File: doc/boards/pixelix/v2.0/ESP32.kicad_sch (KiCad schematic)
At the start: 4 parts

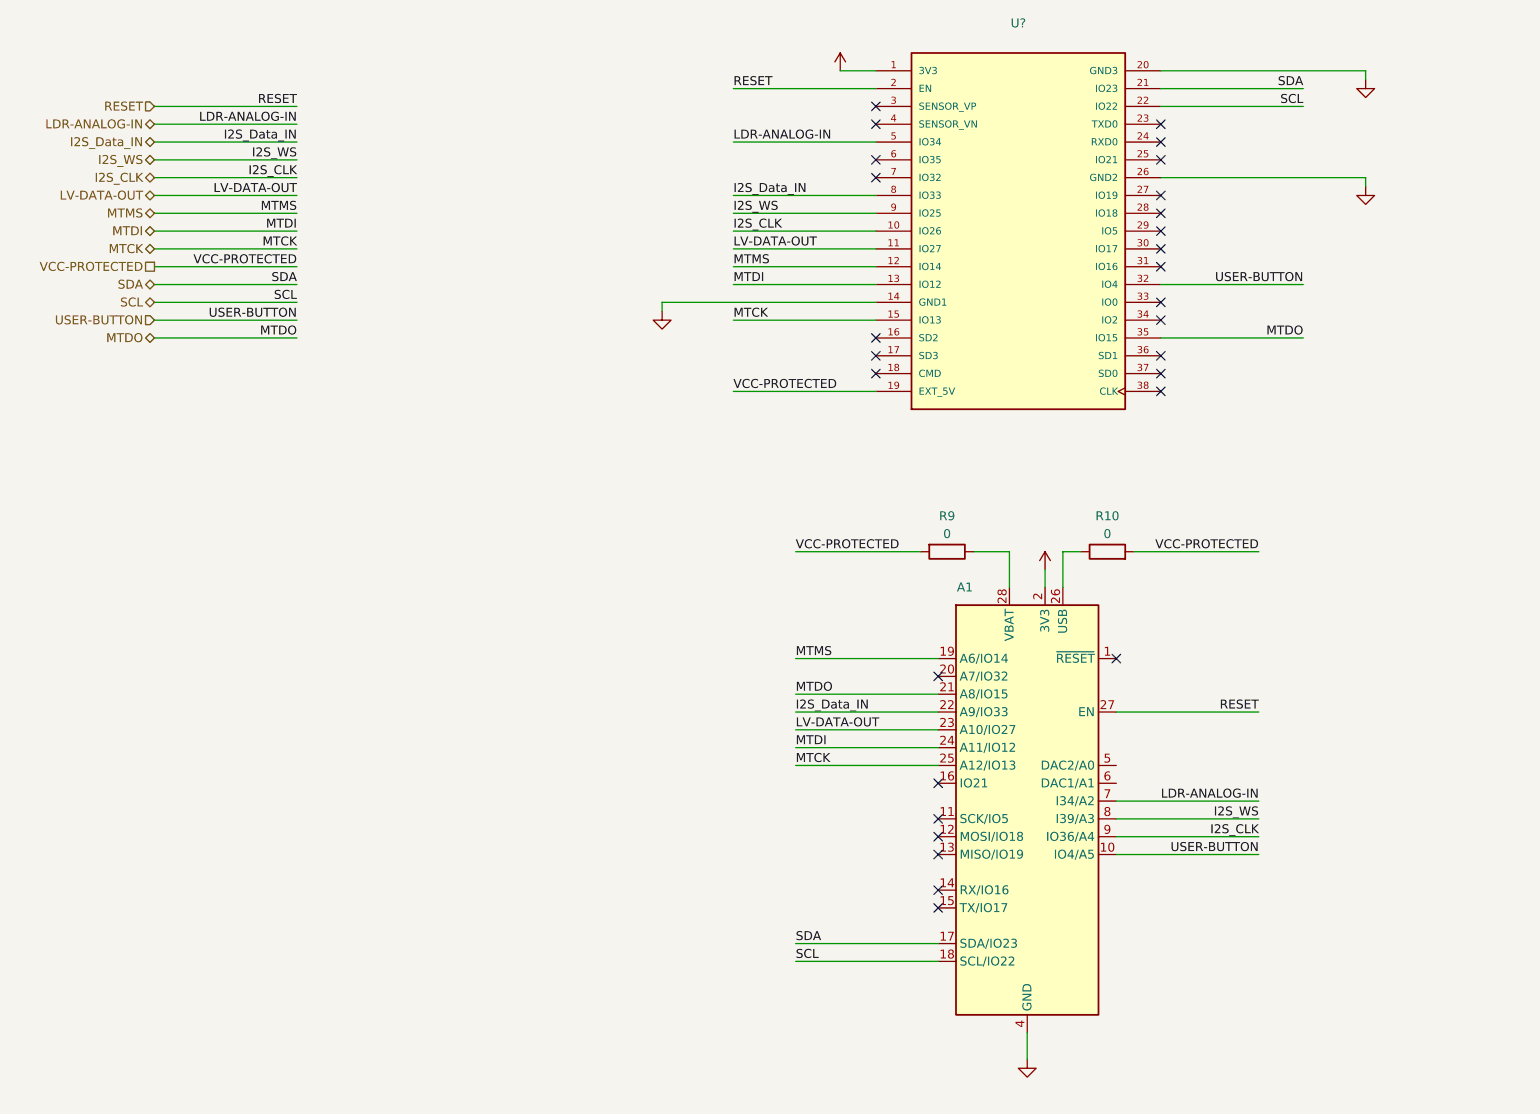
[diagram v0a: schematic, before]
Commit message: Board v2.0 Schematic - add Components (similar to v1.5) - add Pixelix Logo in header
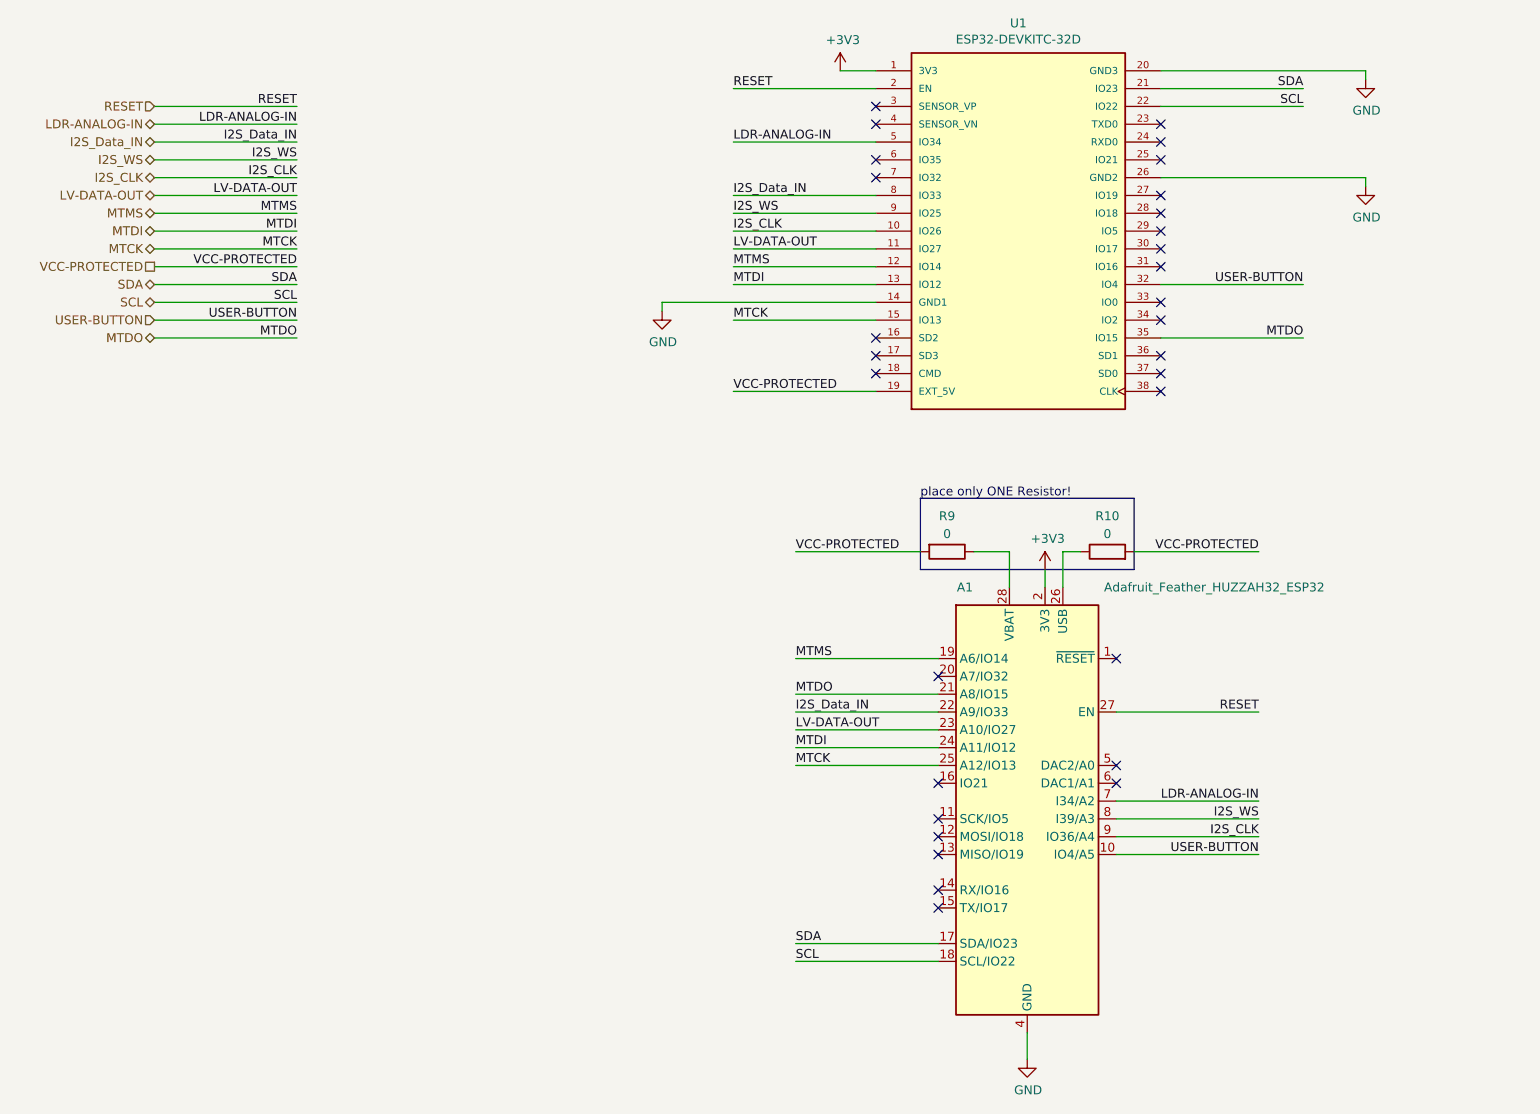
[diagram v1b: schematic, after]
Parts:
- A1: value (none) -> Adafruit_Feather_HUZZAH32_ESP32; footprint (none) -> Module:Adafruit_Feather; Manufacturer (none) -> Adafruit Feather; Part-No. (none) -> HUZZAH32
- R10, R9: footprint (none) -> Resistor_SMD:R_1206_3216Metric_Pad1.30x1.75mm_HandSolder; Manufacturer (none) -> -; Part-No. (none) -> -
- U1: renamed from U?; value (none) -> ESP32-DEVKITC-32D; footprint (none) -> footprints:MODULE_ESP32-DEVKITC-32D; Part-No. (none) -> ESP32-DEVKITC-32D
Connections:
- no-connect marks 28 -> 30
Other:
- note added: "place only ONE Resistor!"
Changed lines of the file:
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@@
   (title_block
     (title "Pixelix")
-    (date "2022-08-05")
+    (date "2022-08-08")
     (rev "2.0")
     (comment 1 "Schneider, Niklas")
@@
   (no_connect (at 139.7 30.48))
   (no_connect (at 180.34 66.04))
+  (no_connect (at 173.99 121.92))
+  (no_connect (at 173.99 124.46))
   (no_connect (at 180.34 55.88))
   (no_connect (at 139.7 60.96))
@@
   (no_connect (at 180.34 40.64))
   (no_connect (at 180.34 35.56))
+  (polyline (pts (xy 146.05 93.98) (xy 176.53 93.98))
+    (stroke (width 0) (type default) (color 0 0 0 0))
+  )
   (wire (pts (xy 57.15 60.96) (xy 36.83 60.96))
     (stroke (width 0) (type default) (color 0 0 0 0))
@@
     (stroke (width 0) (type default) (color 0 0 0 0))
   )
+  (polyline (pts (xy 146.05 83.82) (xy 146.05 93.98))
+    (stroke (width 0) (type default) (color 0 0 0 0))
+  )
   (wire (pts (xy 209.55 38.1) (xy 180.34 38.1))
     (stroke (width 0) (type default) (color 0 0 0 0))
@@
     (stroke (width 0) (type default) (color 0 0 0 0))
   )
+  (polyline (pts (xy 146.05 83.82) (xy 176.53 83.82))
+    (stroke (width 0) (type default) (color 0 0 0 0))
+  )
   (wire (pts (xy 109.22 55.88) (xy 139.7 55.88))
     (stroke (width 0) (type default) (color 0 0 0 0))
@@
     (stroke (width 0) (type default) (color 0 0 0 0))
   )
+  (polyline (pts (xy 176.53 93.98) (xy 176.53 83.82))
+    (stroke (width 0) (type default) (color 0 0 0 0))
+  )
   (wire (pts (xy 128.27 106.68) (xy 148.59 106.68))
     (stroke (width 0) (type default) (color 0 0 0 0))
@@
     (stroke (width 0) (type default) (color 0 0 0 0))
   )
+  (image (at 261.62 173.99) (scale 1.81836)
+    (data
+      iVBORw0KGgoAAAANSUhEUgAAAUoAAABGCAYAAACqnN3KAAAABHNCSVQICAgIfAhkiAAAAAlwSFlz
+      AAAuGAAALhgBKqonIAAAAXpJREFUeJzt3cFqwzAQRVEp///P6io7lzfGE6Sm56zN2NDmgsGDxgAA
+      AAAAAAAAAAAAAAAAaDd3P0CnNcZK18wxZvd15edbhXnzxt+kMG9snbcK8+Zsv66sMG/cmddrFZ5v
+      3ni+9v/n5nkne+1+AIDTCSVAIJQAgVACBEIJEAglQCCUAIFQAgDwzFd8Nf92+uaBzZyrefs2X2zm
+      XM2zmXPFqzdAIJQAgVACBEIJEAglQCCUAIFQAgRCCQDAM1u/ml+FzY15Y3Nj11k4Ve2bOeUbN2/c
+      lO/rzJwnujdz6vfd9fvo7UEnr94AgVACBEIJEAglQCCUAIFQAgRCCRAIJQAAz3zFeRZvp5/h4cyc
+      q3nOzPmNM3PO4dUbIBBKgEAoAQKhBAiEEiAQSoBAKAECoQQA4JlbX823n3Gz6cyc6rxuNnOu5v2F
+      M3O6r6v5b5s5J/fFqzdAIJQAgVACBEIJEAglQCCUAIFQAgRCCQAAAAAAAAAAAAAAAAB8wA+7/5tW
+      3HfTzAAAAABJRU5ErkJggg==
+    )
+  )
+  (text "place only ONE Resistor!" (at 146.05 83.82 0)
+    (effects (font (size 1.27 1.27)) (justify left bottom))
+  )
   (label "MTMS" (at 119.38 50.8 0)
     (effects (font (size 1.27 1.27)) (justify left bottom))
@@
   (symbol (lib_id "ESP32-DEVKITC-32D_new:ESP32-DEVKITC-32D") (at 160.02 45.72 0) (unit 1)
     (in_bom yes) (on_board yes)
-    (property "Reference" "U?" (id 0) (at 160.02 16.0782 0))
-    (property "Value" "" (id 1) (at 160.02 18.3896 0))
-    (property "Footprint" "" (id 2) (at 160.02 45.72 0)
+    (property "Reference" "U1" (id 0) (at 160.02 16.0782 0))
+    (property "Value" "ESP32-DEVKITC-32D" (id 1) (at 160.02 18.3896 0))
+    (property "Footprint" "footprints:MODULE_ESP32-DEVKITC-32D" (id 2) (at 160.02 45.72 0)
       (effects (font (size 1.27 1.27)) (justify left bottom) hide)
     )
@@
     )
     (property "Manufacturer" "Espressif Systems" (id 4) (at 160.02 45.72 0)
+      (effects (font (size 1.27 1.27)) hide)
+    )
+    (property "Part-No." "ESP32-DEVKITC-32D" (id 5) (at 160.02 45.72 0)
       (effects (font (size 1.27 1.27)) hide)
     )
@@
       (effects (font (size 1.27 1.27)) hide)
     )
-    (property "Value" "" (id 1) (at 135.001 18.4658 0))
+    (property "Value" "+3V3" (id 1) (at 135.001 18.4658 0))
     (property "Footprint" "" (id 2) (at 134.62 22.86 0)
       (effects (font (size 1.27 1.27)) hide)
@@
     (in_bom yes) (on_board yes)
     (property "Reference" "A1" (id 0) (at 152.4 96.52 0))
-    (property "Value" "" (id 1) (at 187.96 96.52 0))
-    (property "Footprint" "" (id 2) (at 163.83 161.29 0)
+    (property "Value" "Adafruit_Feather_HUZZAH32_ESP32" (id 1) (at 187.96 96.52 0))
+    (property "Footprint" "Module:Adafruit_Feather" (id 2) (at 163.83 161.29 0)
       (effects (font (size 1.27 1.27)) (justify left) hide)
     )
     (property "Datasheet" "https://cdn-learn.adafruit.com/downloads/pdf/adafruit-huzzah32-esp32-feather.pdf" (id 3) (at 161.29 157.48 0)
+      (effects (font (size 1.27 1.27)) hide)
+    )
+    (property "Manufacturer" "Adafruit Feather" (id 4) (at 161.29 127 0)
+      (effects (font (size 1.27 1.27)) hide)
+    )
+    (property "Part-No." "HUZZAH32" (id 5) (at 161.29 127 0)
       (effects (font (size 1.27 1.27)) hide)
     )
@@
       (effects (font (size 1.27 1.27)) hide)
     )
-    (property "Value" "" (id 1) (at 164.211 89.5858 0))
+    (property "Value" "+3V3" (id 1) (at 164.211 89.5858 0))
     (property "Footprint" "" (id 2) (at 163.83 93.98 0)
       (effects (font (size 1.27 1.27)) hide)
@@
       (effects (font (size 1.27 1.27)) hide)
     )
-    (property "Value" "" (id 1) (at 109.347 61.5442 0))
+    (property "Value" "GND" (id 1) (at 109.347 61.5442 0))
     (property "Footprint" "" (id 2) (at 109.22 57.15 0)
       (effects (font (size 1.27 1.27)) hide)
@@
       (effects (font (size 1.27 1.27)) hide)
     )
-    (property "Value" "" (id 1) (at 209.677 43.7642 0))
+    (property "Value" "GND" (id 1) (at 209.677 43.7642 0))
     (property "Footprint" "" (id 2) (at 209.55 39.37 0)
       (effects (font (size 1.27 1.27)) hide)
@@
       (effects (font (size 1.27 1.27)) hide)
     )
-    (property "Value" "" (id 1) (at 209.677 28.5242 0))
+    (property "Value" "GND" (id 1) (at 209.677 28.5242 0))
     (property "Footprint" "" (id 2) (at 209.55 24.13 0)
       (effects (font (size 1.27 1.27)) hide)
@@
       (effects (font (size 1.27 1.27)) hide)
     )
-    (property "Value" "" (id 1) (at 161.417 168.2242 0))
+    (property "Value" "GND" (id 1) (at 161.417 168.2242 0))
     (property "Footprint" "" (id 2) (at 161.29 163.83 0)
       (effects (font (size 1.27 1.27)) hide)
@@
     (property "Reference" "R9" (id 0) (at 149.86 86.36 90))
     (property "Value" "0" (id 1) (at 149.86 88.9 90))
-    (property "Footprint" "" (id 2) (at 149.86 89.662 90)
+    (property "Footprint" "Resistor_SMD:R_1206_3216Metric_Pad1.30x1.75mm_HandSolder" (id 2) (at 149.86 89.662 90)
       (effects (font (size 1.27 1.27)) hide)
     )
     (property "Datasheet" "~" (id 3) (at 149.86 91.44 0)
+      (effects (font (size 1.27 1.27)) hide)
+    )
+    (property "Manufacturer" "-" (id 4) (at 149.86 91.44 0)
+      (effects (font (size 1.27 1.27)) hide)
+    )
+    (property "Part-No." "-" (id 5) (at 149.86 91.44 0)
       (effects (font (size 1.27 1.27)) hide)
     )
@@
     (property "Reference" "R10" (id 0) (at 172.72 86.36 90))
     (property "Value" "0" (id 1) (at 172.72 88.9 90))
-    (property "Footprint" "" (id 2) (at 172.72 93.218 90)
+    (property "Footprint" "Resistor_SMD:R_1206_3216Metric_Pad1.30x1.75mm_HandSolder" (id 2) (at 172.72 93.218 90)
       (effects (font (size 1.27 1.27)) hide)
     )
@@
       (effects (font (size 1.27 1.27)) hide)
     )
+    (property "Manufacturer" "-" (id 4) (at 172.72 91.44 0)
+      (effects (font (size 1.27 1.27)) hide)
+    )
+    (property "Part-No." "-" (id 5) (at 172.72 91.44 0)
+      (effects (font (size 1.27 1.27)) hide)
+    )

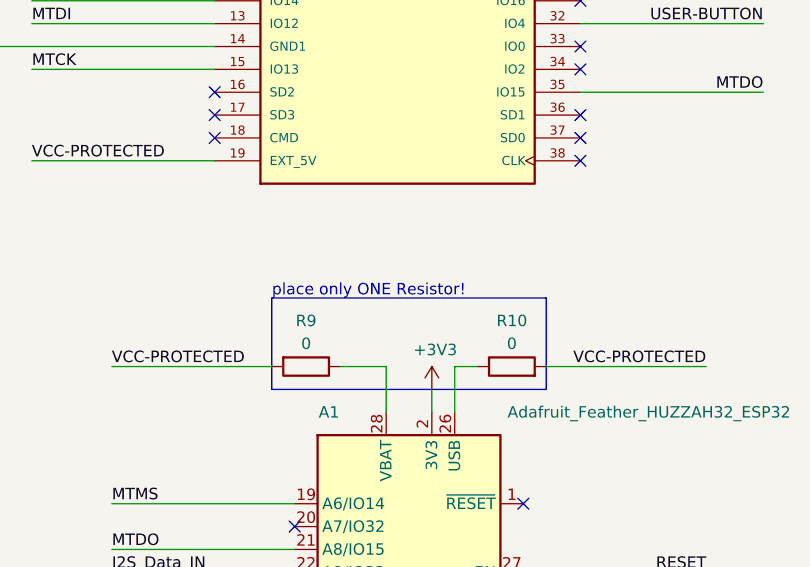
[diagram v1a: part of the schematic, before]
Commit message: Board v2.0 Schematic - add Mounting Holes - some small fixes
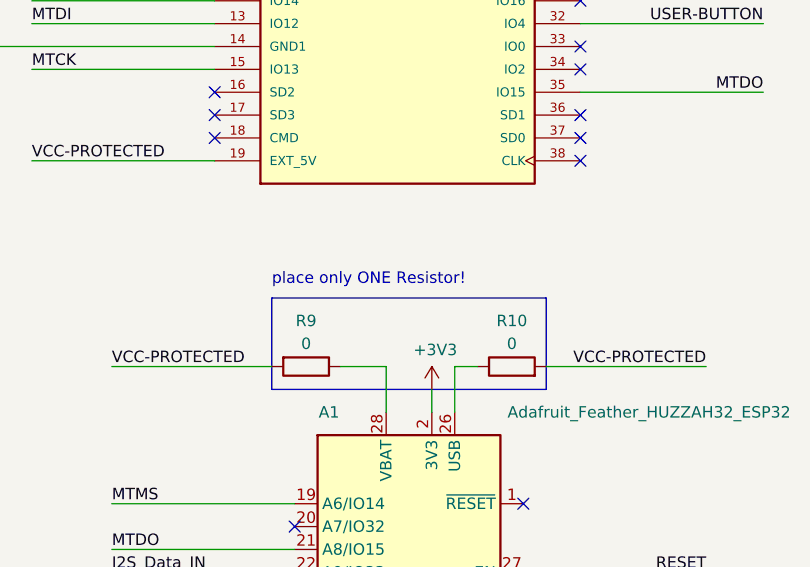
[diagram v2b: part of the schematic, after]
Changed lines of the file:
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@@
     )
   )
-  (text "place only ONE Resistor!" (at 146.05 83.82 0)
+  (text "place only ONE Resistor!" (at 146.05 82.55 0)
     (effects (font (size 1.27 1.27)) (justify left bottom))
   )
